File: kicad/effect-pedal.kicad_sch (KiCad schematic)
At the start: 71 parts, among them J1 USB_C_Receptacle_USB2.0_14P, J4 Conn_01x08, J5 Conn_01x06, J6 Conn_01x06, J7 Conn_ARM_JTAG_SWD_10, J8 NJ3FD-V, J9 NJ3FD-V, Q1 NMOS, Q2 NMOS, SW1 RotaryEncoder_Switch, SW2 RotaryEncoder_Switch, SW3 RotaryEncoder_Switch, SW4 RotaryEncoder_Switch, SW5 SW_Push, SW6 SW_SPDT, SW7 SW_3PDT_x3, U1 STM32H723ZGTx, U2 PCM5102A, U4 USBLC6-2SC6, Y1 Crystal

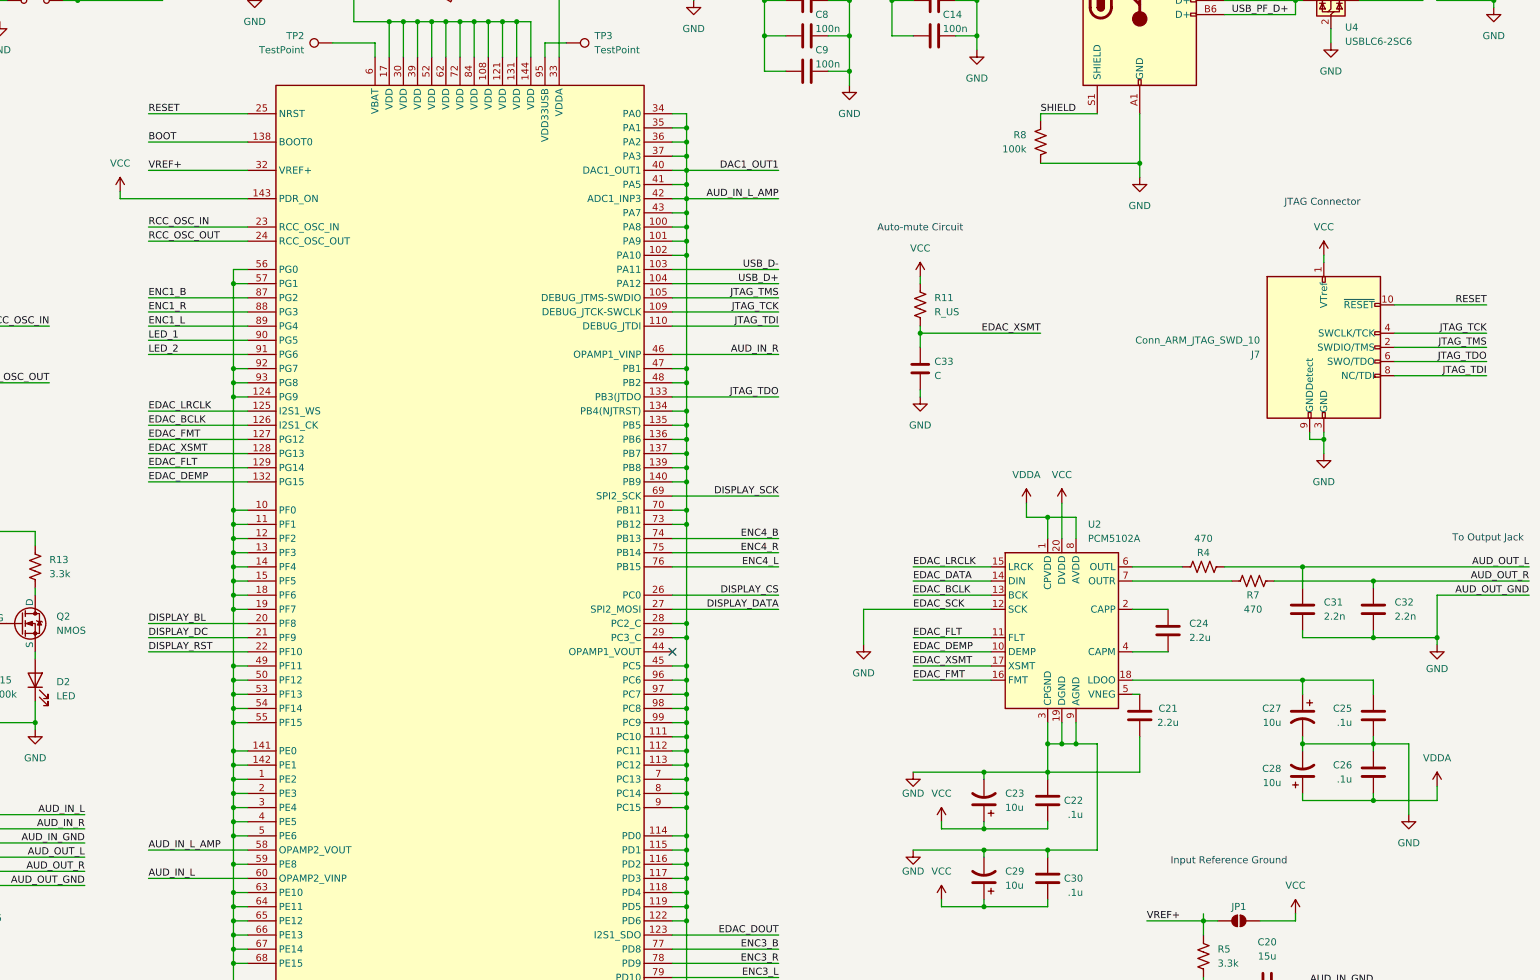
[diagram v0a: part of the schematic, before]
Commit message: Start remapping of pins for I2S6
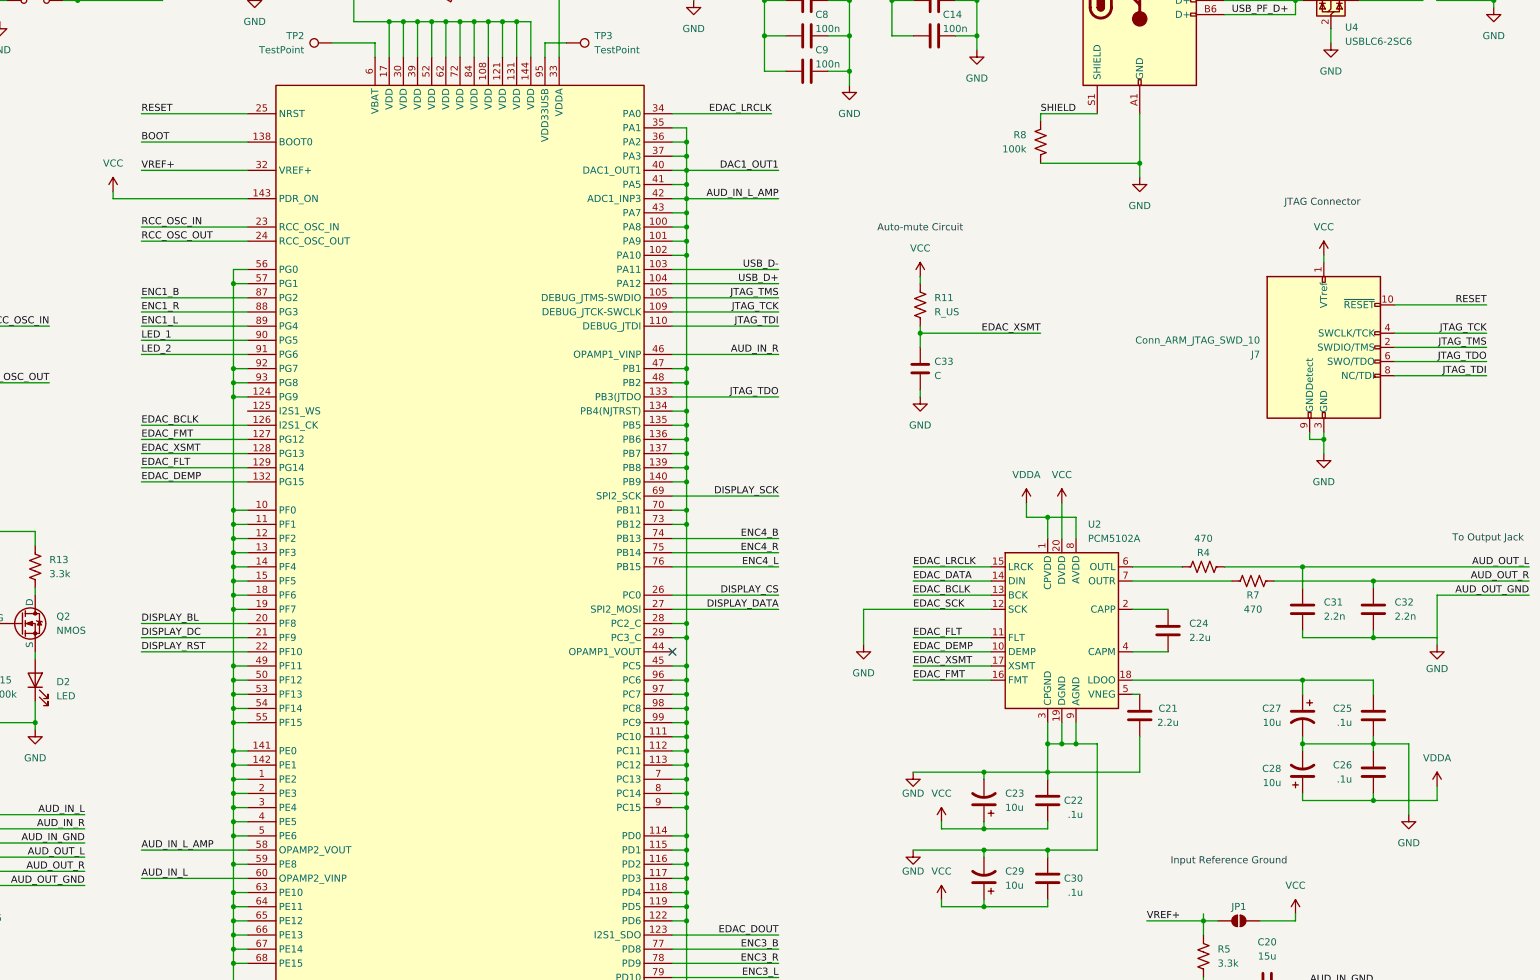
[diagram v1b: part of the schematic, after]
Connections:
- net EDAC_LRCLK: now also U1.34 (PA0); no longer U1.125 (PG10)
- net GND: no longer C31.1, C32.1, U1.34 (PA0)
- new net: C31.1, C32.1

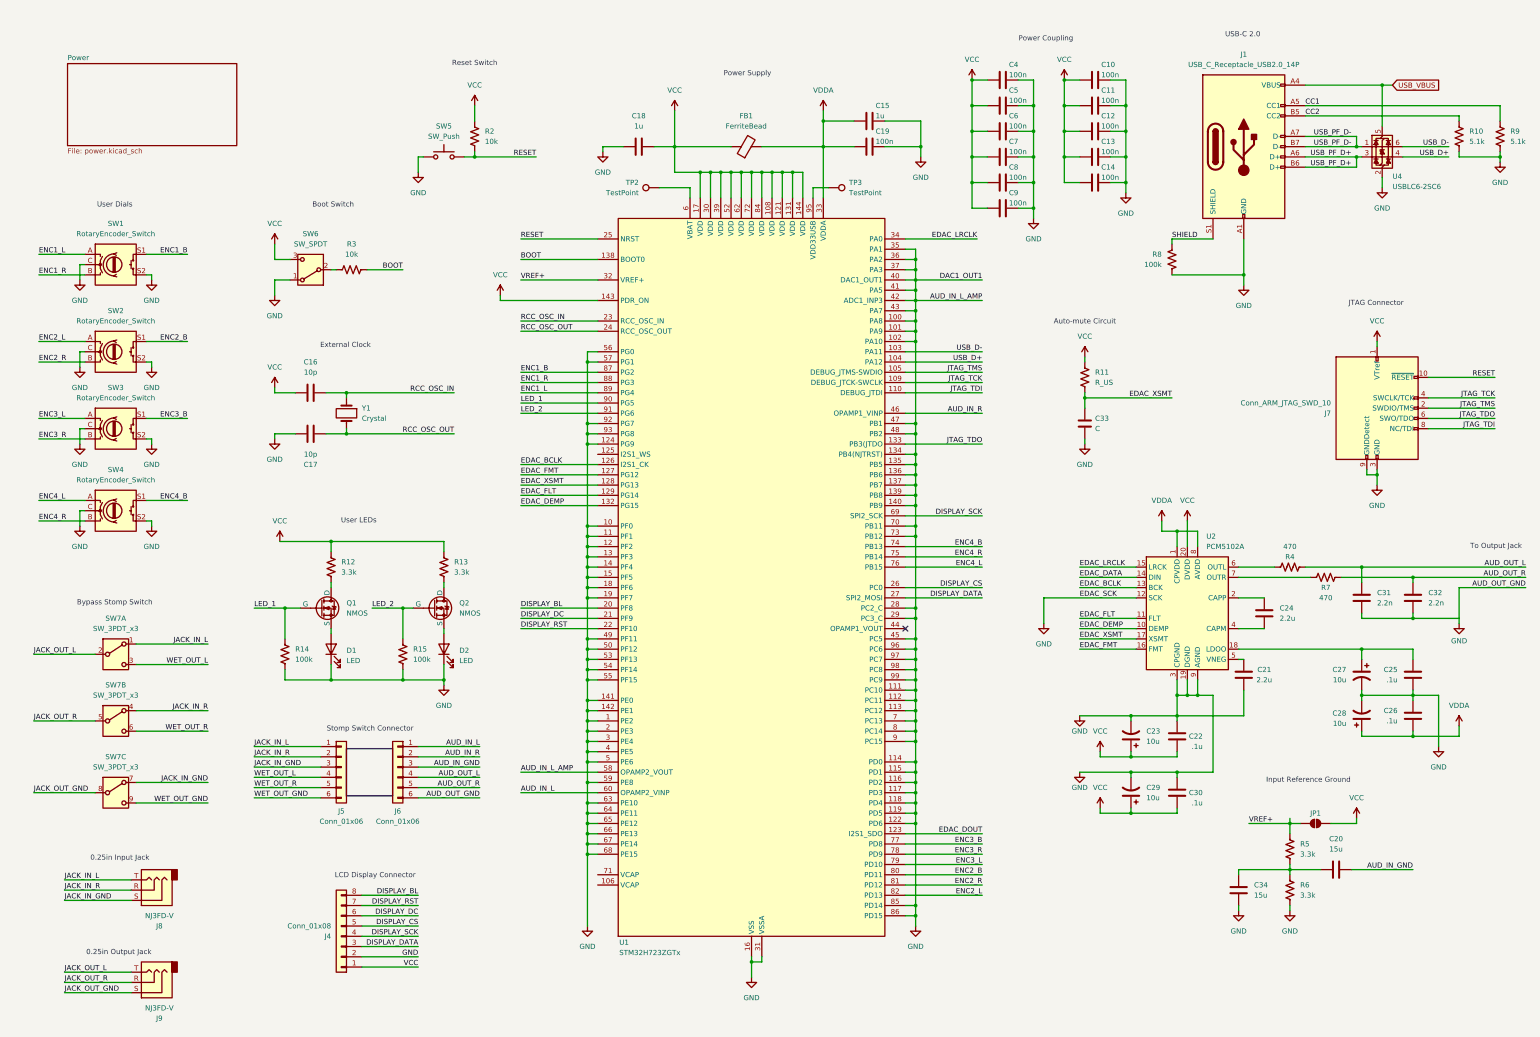
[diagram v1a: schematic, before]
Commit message: Finish schematic and start assigning footprints
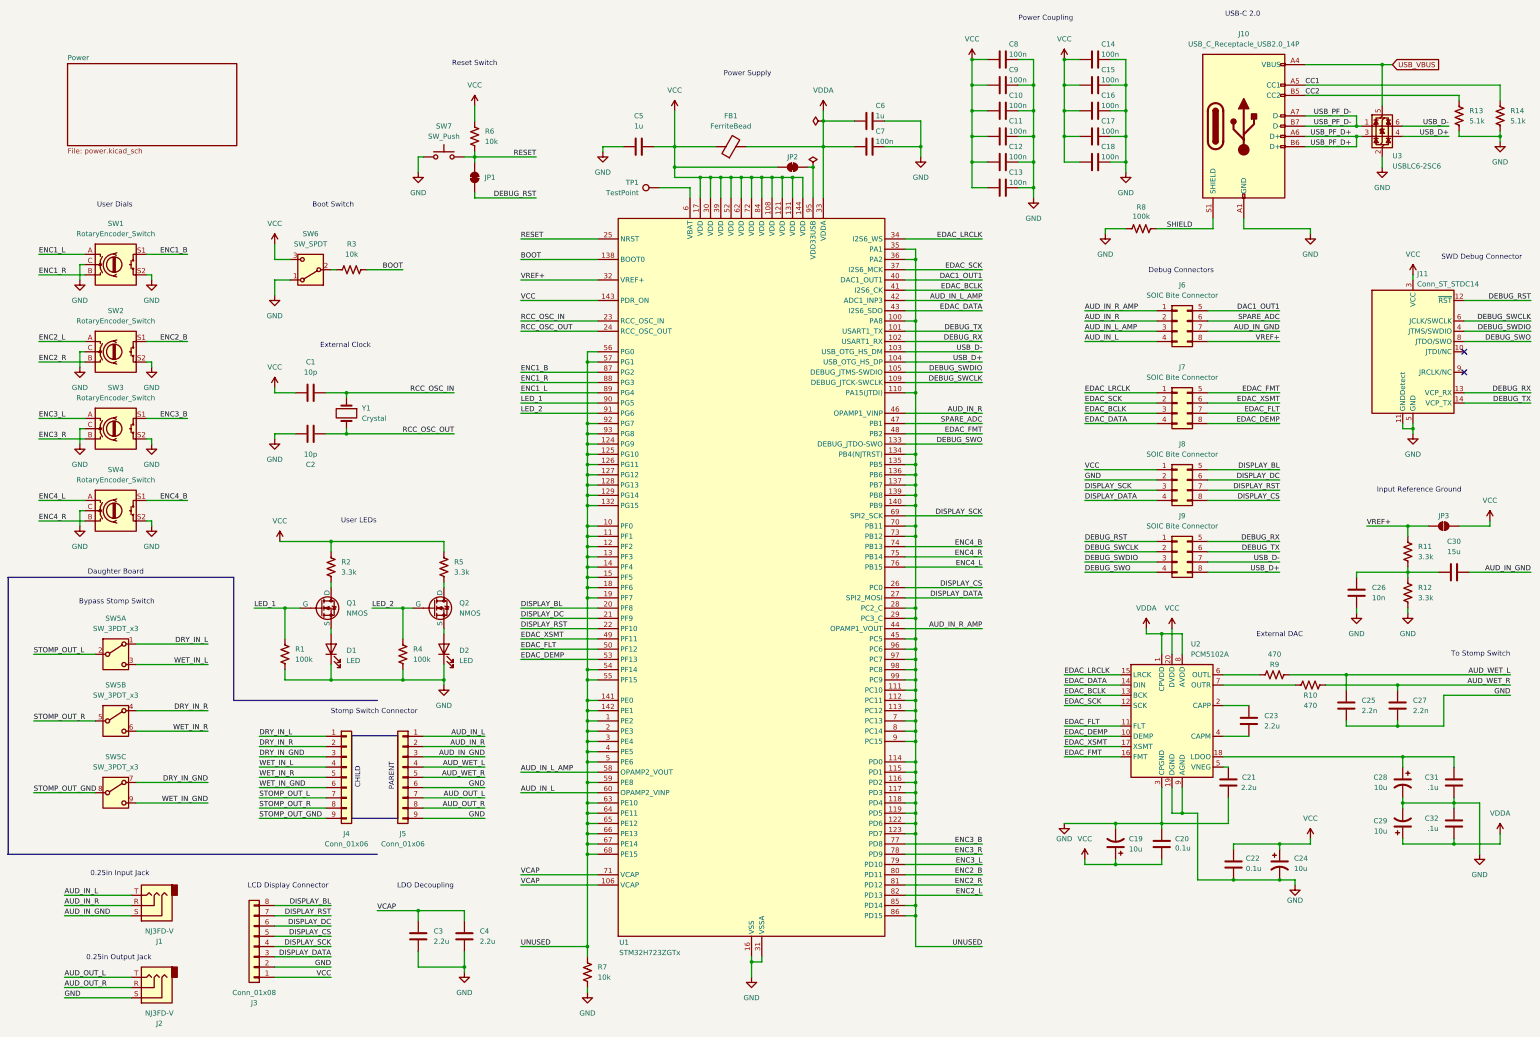
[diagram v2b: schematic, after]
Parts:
- removed C29: 10u, symbol Device:C_Polarized_US
- removed C30: .1u, symbol Device:C
- removed C33: C, KRS_Library:Cap_film, symbol KRS:C
- removed J7: Conn_ARM_JTAG_SWD_10, Connector_PinHeader_1.27mm:PinHeader_2x05_P1.27mm_Vertical, symbol Connector:Conn_ARM_JTAG_SWD_10
- removed R11: R_US, symbol Device:R_US
- removed TP3: TestPoint, symbol Connector:TestPoint
- added C22: 0.1u, Capacitor_SMD:C_0603_1608Metric, symbol Device:C
- added C24: 10u, Capacitor_SMD:C_0603_1608Metric, symbol Device:C_Polarized_US
- added C3, C4: 2.2u, Capacitor_SMD:C_0603_1608Metric, symbol Device:C
- added J11: Conn_ST_STDC14, Connector_TE-Connectivity:TE_MATE-N-LOK_1-770973-x_2x07_P4.14mm_Horizontal, symbol Connector:Conn_ST_STDC14
- added J6, J7, J8, J9: SOIC Bite Connector, SOICBite:SOIC_clipProgSmall, symbol Connector_Generic:Conn_02x04_Top_Bottom
- added JP1, JP2: SolderJumper_2_Bridged, Jumper:SolderJumper-2_P1.3mm_Bridged2Bar_RoundedPad1.0x1.5mm, symbol Jumper:SolderJumper_2_Bridged
- added R7: 10k, Resistor_SMD:R_0603_1608Metric, symbol Device:R_US
- C1: renamed from C16; footprint (none) -> Capacitor_SMD:C_0603_1608Metric
- C10: renamed from C6; footprint (none) -> Capacitor_SMD:C_0603_1608Metric
- C11: renamed from C7; footprint (none) -> Capacitor_SMD:C_0603_1608Metric
- C12: renamed from C8; footprint (none) -> Capacitor_SMD:C_0603_1608Metric
- C13: renamed from C9; footprint (none) -> Capacitor_SMD:C_0603_1608Metric
- C14: renamed from C10; footprint (none) -> Capacitor_SMD:C_0603_1608Metric
- C15: renamed from C11; footprint (none) -> Capacitor_SMD:C_0603_1608Metric
- C16: renamed from C12; footprint (none) -> Capacitor_SMD:C_0603_1608Metric
- C17: renamed from C13; footprint (none) -> Capacitor_SMD:C_0603_1608Metric
- C18: renamed from C14; footprint (none) -> Capacitor_SMD:C_0603_1608Metric
- C19: renamed from C23; footprint (none) -> Capacitor_SMD:C_0603_1608Metric
- C2: renamed from C17; footprint (none) -> Capacitor_SMD:C_0603_1608Metric
- C20: renamed from C22; value .1u -> 0.1u; footprint (none) -> Capacitor_SMD:C_0603_1608Metric
- C21: footprint (none) -> Capacitor_SMD:C_0603_1608Metric
- C23: renamed from C24; footprint (none) -> Capacitor_SMD:C_0603_1608Metric
- C25: renamed from C31; footprint (none) -> Capacitor_SMD:C_0603_1608Metric
- C26: renamed from C34; value 15u -> 10n; footprint (none) -> Capacitor_SMD:C_0603_1608Metric
- C27: renamed from C32; footprint (none) -> Capacitor_SMD:C_0603_1608Metric
- C28: renamed from C27; footprint (none) -> Capacitor_SMD:C_0603_1608Metric
- C29: renamed from C28; footprint (none) -> Capacitor_SMD:C_0603_1608Metric
- C30: renamed from C20; footprint (none) -> Capacitor_SMD:C_0603_1608Metric
- C31: renamed from C25; footprint (none) -> Capacitor_SMD:C_0603_1608Metric
- C32: renamed from C26; footprint (none) -> Capacitor_SMD:C_0603_1608Metric
- C5: renamed from C18; footprint (none) -> Capacitor_SMD:C_0603_1608Metric
- C6: renamed from C15; footprint (none) -> Capacitor_SMD:C_0603_1608Metric
- C7: renamed from C19; footprint (none) -> Capacitor_SMD:C_0603_1608Metric
- C8: renamed from C4; footprint (none) -> Capacitor_SMD:C_0603_1608Metric
- C9: renamed from C5; footprint (none) -> Capacitor_SMD:C_0603_1608Metric
- D1, D2: footprint (none) -> LED_SMD:LED_0805_2012Metric
- FB1: footprint (none) -> Inductor_SMD:L_0603_1608Metric
- J1: renamed from J8; footprint Connector_Audio:Jack_6.35mm_Neutrik_NJ3FD-V_Vertical -> Connector_Audio:Jack_6.35mm_Neutrik_NMJ4HCD2_Horizontal
- J10: renamed from J1; footprint (none) -> Connector_USB:USB_C_Receptacle_GCT_USB4135-GF-A_6P_TopMnt_Horizontal
- J2: renamed from J9; footprint Connector_Audio:Jack_6.35mm_Neutrik_NJ3FD-V_Vertical -> Connector_Audio:Jack_6.35mm_Neutrik_NMJ4HCD2_Horizontal
- J3: renamed from J4; footprint (none) -> Connector_JST:JST_XH_S8B-XH-A_1x08_P2.50mm_Horizontal
- J4: renamed from J5; footprint (none) -> Connector_JST:JST_XH_S9B-XH-A_1x09_P2.50mm_Horizontal; symbol Connector_Generic:Conn_01x06 -> Connector_Generic:Conn_01x09; now left out of the parts list
- J5: renamed from J6; footprint (none) -> Connector_JST:JST_XH_S9B-XH-A_1x09_P2.50mm_Horizontal; symbol Connector_Generic:Conn_01x06 -> Connector_Generic:Conn_01x09
- JP3: renamed from JP1; footprint (none) -> Jumper:SolderJumper-2_P1.3mm_Open_TrianglePad1.0x1.5mm
- Q1, Q2: footprint (none) -> Package_TO_SOT_SMD:SOT-23
- R1: renamed from R14; footprint (none) -> Resistor_SMD:R_0603_1608Metric
- R10: renamed from R7; footprint (none) -> Resistor_SMD:R_0603_1608Metric
- R11: renamed from R5; footprint (none) -> Resistor_SMD:R_0603_1608Metric
- R12: renamed from R6; footprint (none) -> Resistor_SMD:R_0603_1608Metric
- R13: renamed from R10; footprint (none) -> Resistor_SMD:R_0603_1608Metric
- R14: renamed from R9; footprint (none) -> Resistor_SMD:R_0603_1608Metric
- R2: renamed from R12; footprint (none) -> Resistor_SMD:R_0603_1608Metric
- R3, R8: footprint (none) -> Resistor_SMD:R_0603_1608Metric
- R4: renamed from R15; footprint (none) -> Resistor_SMD:R_0603_1608Metric
- R5: renamed from R13; footprint (none) -> Resistor_SMD:R_0603_1608Metric
- R6: renamed from R2; footprint (none) -> Resistor_SMD:R_0603_1608Metric
- R9: renamed from R4; footprint (none) -> Resistor_SMD:R_0603_1608Metric
- SW1, SW2, SW3, SW4: footprint (none) -> Bournes:PEC11L4115FS0020
- SW5: renamed from SW7; now left out of the parts list
- SW6: footprint (none) -> Button_Switch_SMD:SW_SPST_B3S-1100
- SW7: renamed from SW5; footprint (none) -> Button_Switch_THT:SW_PUSH_6mm
- TP1: renamed from TP2; footprint (none) -> TestPoint:TestPoint_Pad_2.0x2.0mm
- Y1: footprint (none) -> Crystal:Crystal_SMD_HC49-SD
- renumbered U4 to U3
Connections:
- net EDAC_DOUT is gone; now on net UNUSED: U1.123 (PD7)
- net JTAG_TDI is gone; now on net UNUSED: U1.110 (PA15(JTDI))
- net AUD_IN_GND: now also J1.S, J6.7 (Pin_7)
- net AUD_IN_L: now also J1.T, J6.4 (Pin_4)
- net AUD_IN_R: now also J1.R, J6.2 (Pin_2)
- net AUD_OUT_L: now also J2.T, J5.7 (Pin_7); no longer C25.2, J5.4 (Pin_4), R9.1
- net AUD_OUT_R: now also J2.R, J5.8 (Pin_8); no longer C27.2, J5.5 (Pin_5), R10.2
- net DISPLAY_BL: now also J8.5 (Pin_5)
- net DISPLAY_CS: now also J8.8 (Pin_8)
- net DISPLAY_DATA: now also J8.4 (Pin_4)
- net DISPLAY_DC: now also J8.6 (Pin_6)
- net DISPLAY_RST: now also J8.7 (Pin_7)
- net DISPLAY_SCK: now also J8.3 (Pin_3)
- net EDAC_BCLK: now also U1.41 (PA5), J7.3 (Pin_3); no longer U1.126 (PG11)
- net EDAC_DATA: now also U1.43 (PA7), J7.4 (Pin_4)
- net EDAC_DEMP: now also U1.53 (PF13), J7.8 (Pin_8); no longer U1.132 (PG15)
- net EDAC_FLT: now also U1.50 (PF12), J7.7 (Pin_7); no longer U1.129 (PG14)
- net EDAC_FMT: now also U1.48 (PB2), J7.5 (Pin_5); no longer U1.127 (PG12)
- net EDAC_LRCLK: now also J7.1 (Pin_1)
- net EDAC_XSMT: now also U1.49 (PF11), J7.6 (Pin_6); no longer U1.128 (PG13)
- net GND: now also C25.1, C27.1, J2.S, J5.9 (Pin_9), R8.1, C22.2, C24.2, C3.2, C4.2, J11.11 (GNDDetect), J11.5 (GND), J11.7 (GND), J8.2 (Pin_2), R7.2; no longer R8.2, U1.1 (PE2), U1.10 (PF0), U1.100 (PA8), U1.101 (PA9), U1.102 (PA10), U1.11 (PF1), U1.111 (PC10), U1.112 (PC11), U1.113 (PC12), U1.114 (PD0), U1.115 (PD1), U1.116 (PD2), U1.117 (PD3), U1.118 (PD4), U1.119 (PD5), U1.12 (PF2), U1.122 (PD6), U1.124 (PG9), U1.13 (PF3), U1.134 (PB4(NJTRST)), U1.135 (PB5), U1.136 (PB6), U1.137 (PB7), U1.139 (PB8), U1.14 (PF4), U1.140 (PB9), U1.141 (PE0), U1.142 (PE1), U1.15 (PF5), U1.18 (PF6), U1.19 (PF7), U1.2 (PE3), U1.28 (PC2_C), U1.29 (PC3_C), U1.3 (PE4), U1.35 (PA1), U1.36 (PA2), U1.37 (PA3), U1.4 (PE5), U1.40 (PA4), U1.41 (PA5), U1.42 (PA6), U1.43 (PA7), U1.45 (PC5), U1.47 (PB1), U1.48 (PB2), U1.49 (PF11), U1.5 (PE6), U1.50 (PF12), U1.53 (PF13), U1.54 (PF14), U1.55 (PF15), U1.56 (PG0), U1.57 (PG1), U1.58 (PE7), U1.59 (PE8), U1.63 (PE10), U1.64 (PE11), U1.65 (PE12), U1.66 (PE13), U1.67 (PE14), U1.68 (PE15), U1.7 (PC13), U1.70 (PB11), U1.73 (PB12), U1.8 (PC14), U1.85 (PD14), U1.86 (PD15), U1.9 (PC15), U1.92 (PG7), U1.93 (PG8), U1.96 (PC6), U1.97 (PC7), U1.98 (PC8), U1.99 (PC9), U2.12 (SCK)
- net RESET: now also JP1.2 (B)
- net SHIELD: now also R8.2; no longer R8.1
- net USB_D+: now also J9.8 (Pin_8)
- net USB_D-: now also J9.7 (Pin_7)
- net VCC: now also C22.1, C24.1, J11.3 (VCC), J8.1 (Pin_1), JP2.1 (A)
- net VREF+: now also J6.8 (Pin_8)
- net VCAP: now reaches U1.106 (VCAP)
- net VCAP: now also U1.71 (VCAP), C3.1, C4.1
- net UNUSED: now reaches U1.125 (PG10)
- net UNUSED: now also U1.1 (PE2), U1.10 (PF0), U1.100 (PA8), U1.11 (PF1), U1.111 (PC10), U1.112 (PC11), U1.113 (PC12), U1.114 (PD0), U1.115 (PD1), U1.116 (PD2), U1.117 (PD3), U1.118 (PD4), U1.119 (PD5), U1.12 (PF2), U1.122 (PD6), U1.124 (PG9), U1.126 (PG11), U1.127 (PG12), U1.128 (PG13), U1.129 (PG14), U1.13 (PF3), U1.132 (PG15), U1.134 (PB4(NJTRST)), U1.135 (PB5), U1.136 (PB6), U1.137 (PB7), U1.139 (PB8), U1.14 (PF4), U1.140 (PB9), U1.141 (PE0), U1.142 (PE1), U1.15 (PF5), U1.18 (PF6), U1.19 (PF7), U1.2 (PE3), U1.28 (PC2_C), U1.29 (PC3_C), U1.3 (PE4), U1.35 (PA1), U1.36 (PA2), U1.4 (PE5), U1.45 (PC5), U1.5 (PE6), U1.54 (PF14), U1.55 (PF15), U1.56 (PG0), U1.57 (PG1), U1.59 (PE8), U1.63 (PE10), U1.64 (PE11), U1.65 (PE12), U1.66 (PE13), U1.67 (PE14), U1.68 (PE15), U1.7 (PC13), U1.70 (PB11), U1.73 (PB12), U1.8 (PC14), U1.85 (PD14), U1.86 (PD15), U1.9 (PC15), U1.92 (PG7), U1.93 (PG8), U1.96 (PC6), U1.97 (PC7), U1.98 (PC8), U1.99 (PC9), R7.1
- net AUD_IN_R_AMP: now reaches U1.44 (PC4)
- net AUD_IN_R_AMP: now also J6.1 (Pin_1)
- net at U1.95 (VDD33USB): now also JP2.2 (B)
- net JACK_IN_GND renamed DRY_IN_GND
- net DRY_IN_GND: no longer J1.S
- net JACK_IN_L renamed DRY_IN_L
- net DRY_IN_L: no longer J1.T
- net JACK_IN_R renamed DRY_IN_R
- net DRY_IN_R: no longer J1.R
- net JACK_OUT_GND renamed STOMP_OUT_GND
- net STOMP_OUT_GND: now also J4.9 (Pin_9); no longer J2.S
- net JACK_OUT_L renamed STOMP_OUT_L
- net STOMP_OUT_L: now also J4.7 (Pin_7); no longer J2.T
- net JACK_OUT_R renamed STOMP_OUT_R
- net STOMP_OUT_R: now also J4.8 (Pin_8); no longer J2.R
- net JTAG_TCK renamed DEBUG_SWCLK
- net DEBUG_SWCLK: now also J11.6 (JCLK/SWCLK), J9.2 (Pin_2)
- net JTAG_TDO renamed DEBUG_SWO
- net DEBUG_SWO: now also J11.8 (JTDO/SWO), J9.4 (Pin_4)
- net JTAG_TMS renamed DEBUG_SWDIO
- net DEBUG_SWDIO: now also J11.4 (JTMS/SWDIO), J9.3 (Pin_3)
- net WET_OUT_GND renamed WET_IN_GND
- net WET_OUT_L renamed WET_IN_L
- net WET_OUT_R renamed WET_IN_R
- new net AUD_IN_L_AMP: J6.3 (Pin_3), U1.42 (PA6), U1.58 (PE7)
- new net AUD_WET_L: C25.2, J5.4 (Pin_4), R9.1
- new net AUD_WET_R: C27.2, J5.5 (Pin_5), R10.2
- new net DAC1_OUT1: J6.5 (Pin_5), U1.40 (PA4)
- new net DEBUG_RST: J11.12 (~{RST}), J9.1 (Pin_1), JP1.1 (A)
- new net DEBUG_RX: J11.13 (VCP_RX), J9.5 (Pin_5), U1.102 (PA10)
- new net DEBUG_TX: J11.14 (VCP_TX), J9.6 (Pin_6), U1.101 (PA9)
- new net EDAC_SCK: J7.2 (Pin_2), U1.37 (PA3), U2.12 (SCK)
- new net SPARE_ADC: J6.6 (Pin_6), U1.47 (PB1)
- no-connect marks 1 -> 2
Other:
- note added: "CHILD"
- note added: "Daughter Board"
- note added: "Debug Connectors"
- note added: "External DAC"
- note added: "LDO Decoupling"
- note added: "PARENT"
- note added: "SWD Debug Connector"
- note added: "To Stomp Switch"
- note removed: "Auto-mute Circuit"
- note removed: "JTAG Connector"
- note removed: "To Output Jack"
- moved on the sheet: C10, C11, C12, C13, C14, C15, C16, C17, C18, C19, C20, C21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

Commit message: DNP markers
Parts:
- C1, C2, Y1: now not fitted
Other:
- moved on the sheet: R8

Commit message: Add more part numbers and VDDA regulator
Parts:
- removed C19: 10u, Capacitor_SMD:C_0603_1608Metric, symbol Device:C_Polarized_US
- removed C20: 0.1u, Capacitor_SMD:C_0603_1608Metric, symbol Device:C
- added C21: 0.1u, Capacitor_SMD:C_0603_1608Metric, symbol Device:C
- added C25: 10u, Capacitor_SMD:C_0603_1608Metric, symbol Device:C_Polarized_US
- added C27: 1u, Capacitor_SMD:C_0603_1608Metric, symbol Device:C
- added C34: 10u, Capacitor_SMD:C_0603_1608Metric, symbol Device:C
- added TP1, TP2, TP3, TP4: TestPoint, TestPoint:TestPoint_Pad_2.0x2.0mm, symbol Connector:TestPoint
- C1, C2: Part (none) -> KGM15ACG1E100KT; now fitted
- C10, C11, C12, C13, C14, C15, C16, C17, C18, C7, C8, C9: value 100n -> 0.1u; Part (none) -> GMK107BJ104MAHT
- C19: renamed from C22; Part (none) -> GMK107BJ104MAHT
- C20: renamed from C21; Part (none) -> LMK107BJ225KAHT
- C22: renamed from C23; Part (none) -> LMK107BJ225KAHT
- C23: renamed from C24; Part (none) -> LMK107BBJ106KALT
- C24: renamed from C26; Part (none) -> HMJ107BB7103KAHT
- C26: renamed from C25; Part (none) -> HMK107B7222KAHT
- C28: renamed from C27; Part (none) -> HMK107B7222KAHT
- C29: renamed from C28; Part (none) -> LMK107BBJ106KALT
- C3, C4: Part (none) -> LMK107BJ225KAHT
- C30: renamed from C29; Part (none) -> LMK107BBJ106KALT
- C31, C32: value .1u -> 0.1u; Part (none) -> GMK107BJ104MAHT
- C33: renamed from C30; value 15u -> 10u; Part (none) -> LMK107BBJ106KALT
- C5, C6: Part (none) -> JMK107BJ105KAHT
- D1, D2: Part (none) -> QBLP631-R
- FB1: footprint Inductor_SMD:L_0603_1608Metric -> Inductor_SMD:L_1206_3216Metric; Part (none) -> CZP2BFTTE601P
- J1, J2: footprint Connector_Audio:Jack_6.35mm_Neutrik_NMJ4HCD2_Horizontal -> Connector_Audio:Jack_6.35mm_Neutrik_NMJ6HCD3_Horizontal; Part (none) -> NMJ6HCD3
- J10: footprint Connector_USB:USB_C_Receptacle_GCT_USB4135-GF-A_6P_TopMnt_Horizontal -> (none); Part (none) -> 2169900002
- J3, J4, J5, J6, J7, J8, J9, R1, R10, R11, R12, R13, R14, R2, R3, R4, R5, R6, R7, R8, R9: Part (none) -> Generic
- SW1, SW2, SW3, SW4: footprint Bournes:PEC11L4115FS0020 -> Rotary_Encoder:RotaryEncoder_Bourns_Vertical_PEC12R-3x17F-Sxxxx; Part (none) -> PEC12R-4225F-S0024
- U1: Part (none) -> STM32H723ZGT6TR
- U2: Part (none) -> PCM5102AQPWRQ1
- U3: Part (none) -> USBLC6-2SC6
- renumbered TP1 to TP5
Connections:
- net AUD_IN_GND: now also C34.2
- net GND: now also C21.2, C25.2, C27.1, TP4.1
- net VCC: now also C21.1, C25.1, TP1.1
- net VDDA: now also TP2.1
- net VREF+: now also C27.2, TP3.1
- net at C24.2, C33.1, R11.2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: now also C34.1
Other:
- sheet Power ports: added VCC, VDDA; removed none
- note added: "Microcontroller Power Supply"
- note added: "Rail Test Points"
- company: (none) -> ECE 212 Group 2
- title: (none) -> Digital Effect Pedal
- moved on the sheet: C19, C23, C24, C33
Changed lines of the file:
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@@
 	(generator_version "9.0")
 	(paper "A3")
+	(title_block
+		(title "Digital Effect Pedal")
+		(date "2026-02-18")
+		(rev "1")
+		(company "ECE 212 Group 2")
+	)

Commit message: Add more parts
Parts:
- Q1, Q2: Part (none) -> AO3400
- SW6: Part (none) -> SLW-105558-2A-N-D
